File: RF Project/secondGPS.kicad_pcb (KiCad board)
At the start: 2 copper layers, 30 x 55 mm, 36 parts, among them J1 CONN_Right, J2 CONN_Left, U1 CC2500RGPR, U11 Venus634SMD, U2 U.FL_male, U3 U.FL_male

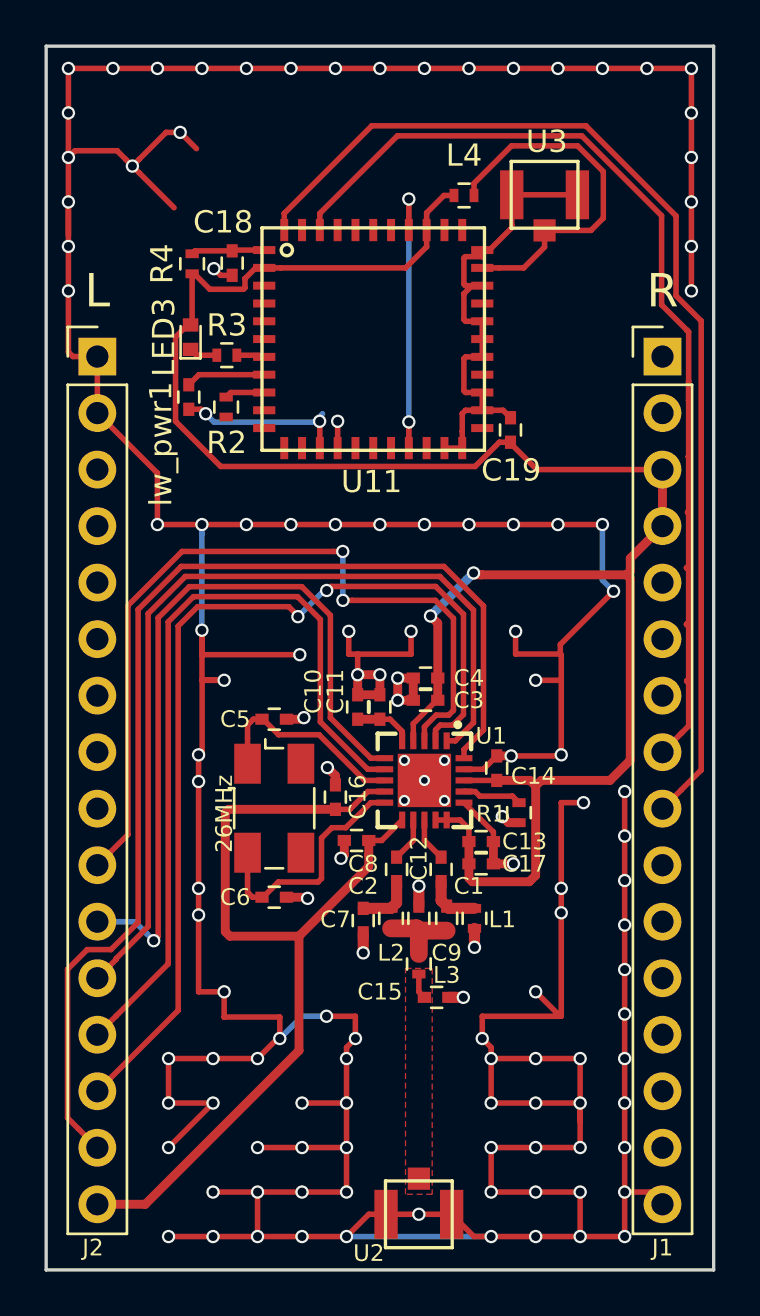
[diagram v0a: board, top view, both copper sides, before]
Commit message: revision component placement, coupling caps added
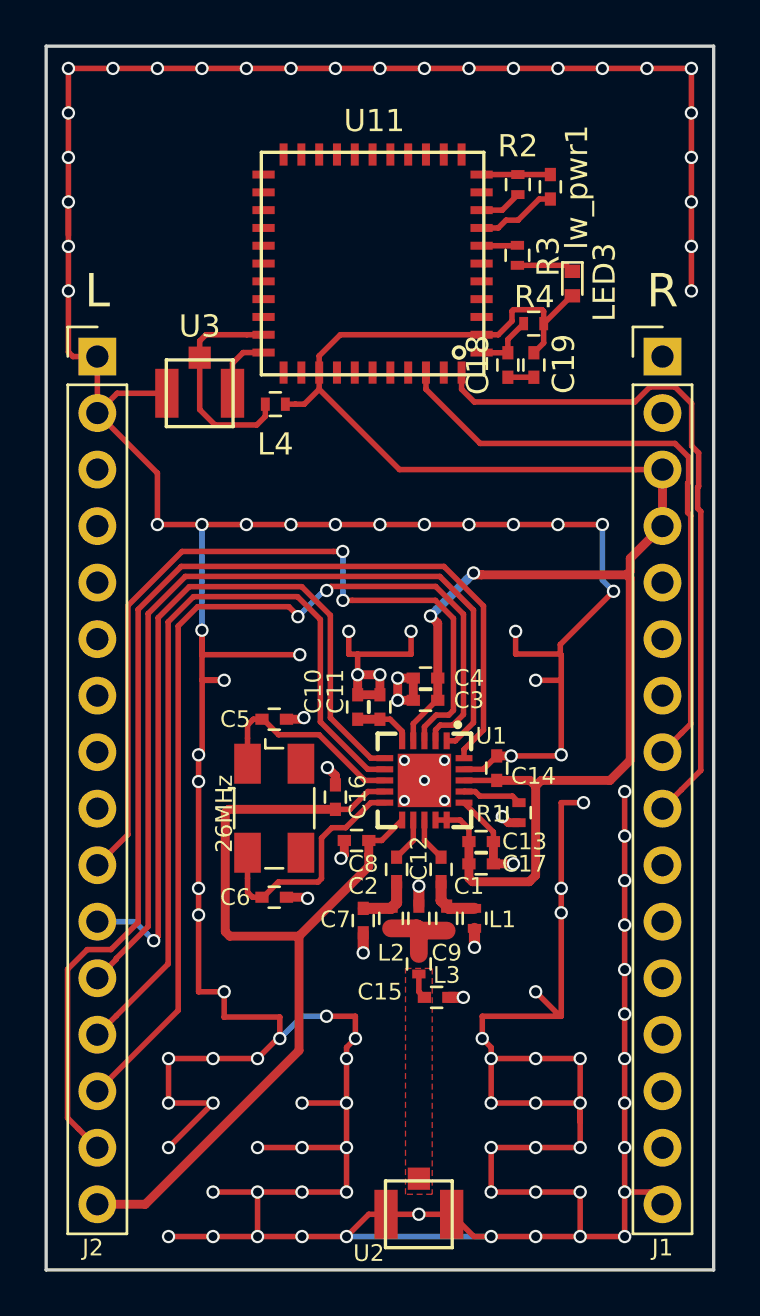
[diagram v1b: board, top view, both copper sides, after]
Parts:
- moved lw_pwr1 18.8 mm to (107.7, 78.8), turned to 90 degrees
- moved U3 17.9 mm to (91.9, 88.1), turned to 180 degrees
- moved LED3 17.3 mm to (108.7, 83.2), turned to 270 degrees
- moved R2 16.5 mm to (106.2, 78.7), turned to 90 degrees
- moved R4 15.6 mm to (106.9, 85.0), turned to 180 degrees
- moved R3 13.8 mm to (106.2, 81.9), turned to 90 degrees
- moved C18 13.2 mm to (105.8, 86.8)
- moved L4 12.6 mm to (95.3, 88.6), turned to 180 degrees
- moved U11 10.8 mm to (104.6, 86.3), turned to 180 degrees
- moved C19 3.10 mm to (106.9, 86.8), turned to 90 degrees
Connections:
- C19 pad 1: RF_GND -> PWR_GND
- U11 pad 21: RF_GND -> PWR_GND
- U11 pad 22: RF_GND -> PWR_GND
- U11 pad 24: RF_GND -> PWR_GND
- U11 pad 25: RF_GND -> PWR_GND
- U11 pad 27: RF_GND -> PWR_GND
- U11 pad 28: RF_GND -> PWR_GND
- U11 pad 29: RF_GND -> PWR_GND
- U11 pad 31: RF_GND -> PWR_GND
- U11 pad 33: RF_GND -> PWR_GND
- U3 pad 1: RF_GND -> PWR_GND
- U3 pad 2: RF_GND -> PWR_GND
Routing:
- net RF_GND: track 22.6 -> 0.00 mm
- net PWR_GND: track 340.2 -> 317.8 mm, vias 134 -> 126
- net TX: track 49.5 -> 31.0 mm
- net RX: track 44.5 -> 27.7 mm
- net AVDD: track 136.1 -> 125.7 mm
- net /GPS/RFIN: track 16.4 -> 10.0 mm
- net Net-(LED3-Pad1): track 1.29 -> 2.58 mm
- net /GPS/RSTN: track 3.31 -> 2.79 mm
